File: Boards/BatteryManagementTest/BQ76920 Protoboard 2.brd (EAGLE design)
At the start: 51 x 52 mm, 16 parts, among them U1 BQ7692006PWRPW20-M, U2 STD20NF06LDPAK-M

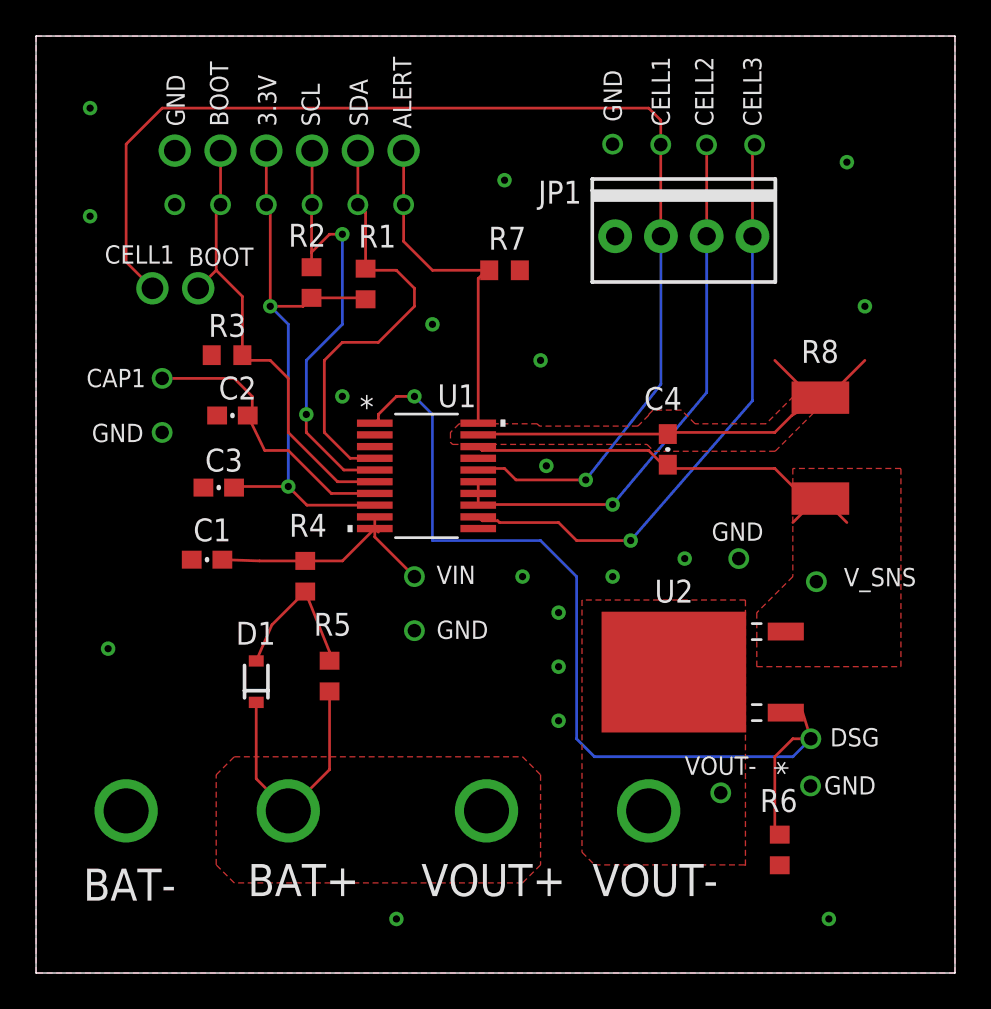
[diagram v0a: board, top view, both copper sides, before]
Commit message: added final rev2 protoboard for BQ76920
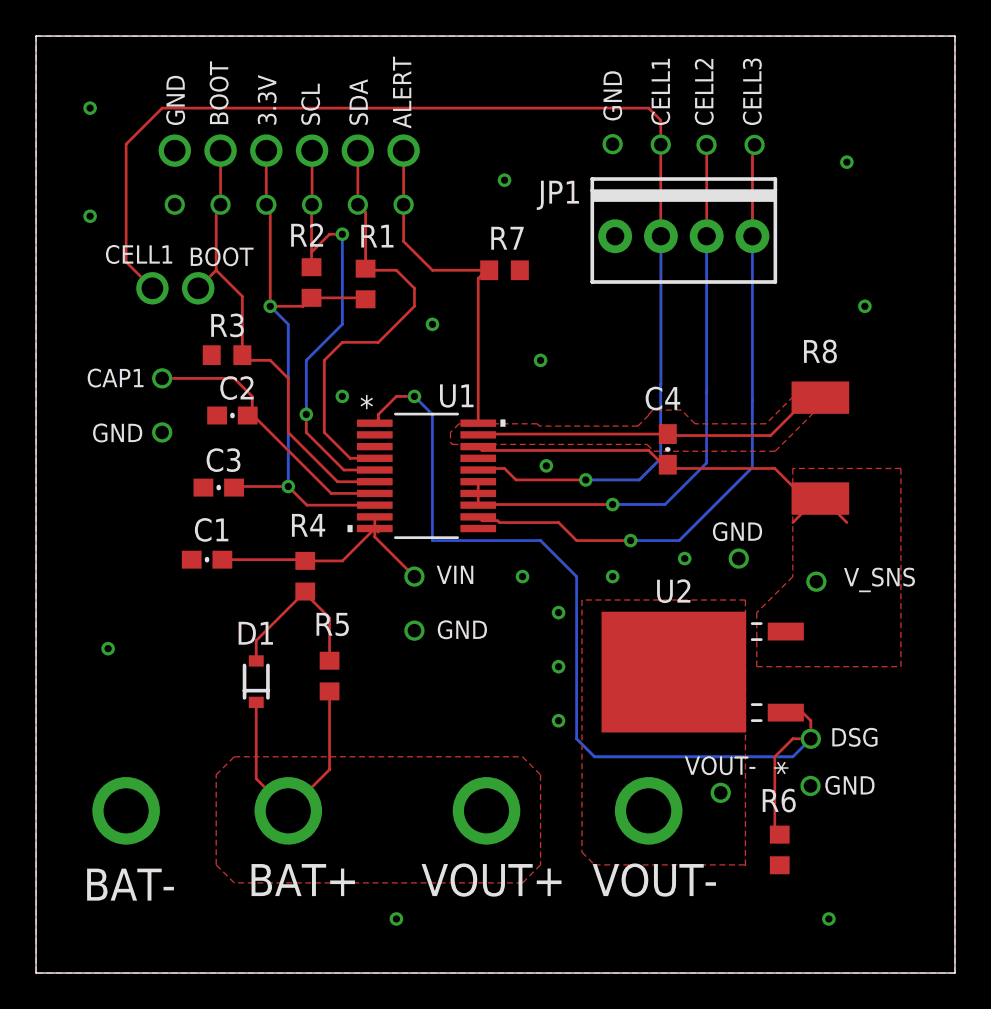
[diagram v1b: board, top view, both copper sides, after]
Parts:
- R8: value (none) -> 50m
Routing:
- net GND: track 26.4 -> 19.9 mm
- net BCELL1: track 67.1 -> 69.1 mm
- net BCELL2: track 30.6 -> 32.6 mm
- net BCELL3: track 33.5 -> 35.4 mm
- net CAP1: track 15.8 -> 15.3 mm
